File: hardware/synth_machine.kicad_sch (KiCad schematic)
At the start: 93 parts, among them J1 USB-C (MIDI + 5V power), J10 Pot WAV (10k lin, panel) JST-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, J11 Pot ATK (10k lin, panel) JST-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, J12 Pot DEC (10k lin, panel) JST-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, J13 Pot SUS (10k lin, panel) JST-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, J14 Pot REL (10k lin, panel) JST-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, J5 Speaker L (JST-PH), J6 Speaker R (JST-PH), J7 Headphones 3.5mm (CUI SJ1-351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, J8 Expansion, K1 KEY C4 (direct D10) JST-XH, K10 A4 [c2 r2] JST-XH, K11 A#4 [c1 r1] JST-XH, K12 B4 [c1 r2] JST-XH, K13 C5 [c0 r2] JST-XH, K14 BTN1 [c0 r0] JST-XH, K15 BTN2 [c0 r1] JST-XH, K16 BTN3 [c1 r0] JST-XH, K17 BTN4 [c2 r0] JST-XH, K18 BTN5 [c3 r0] JST-XH, K19 BTN6 [c4 r0] JST-XH, K2 C#4 [c5 r0] JST-XH, K3 D4 [c5 r1] JST-XH, K4 D#4 [c4 r1] JST-XH, K5 E4 [c5 r2] JST-XH, K6 F4 [c4 r2] JST-XH, K7 F#4 [c3 r1] JST-XH, K8 G4 [c3 r2] JST-XH, K9 G#4 [c2 r1] JST-XH, Q1 MMBT3904, U1 Daisy Seed / Seed3, U2 TPA6138A2PWR, U3 MAX98306ETD+T

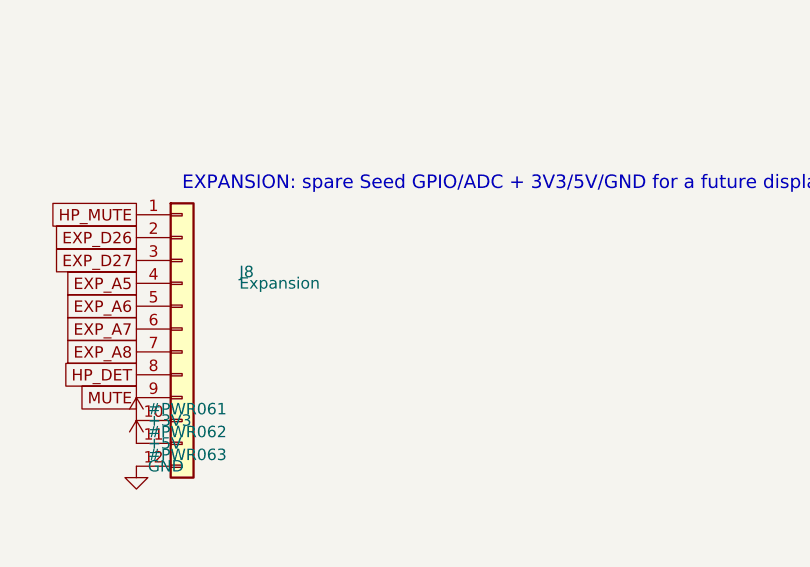
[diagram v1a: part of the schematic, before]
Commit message: J8 expansion header becomes a 1x12 female socket; Digi-Key list sized for two boards
Co-Authored-By: Claude Fable 5.1 <noreply@anthropic.com>
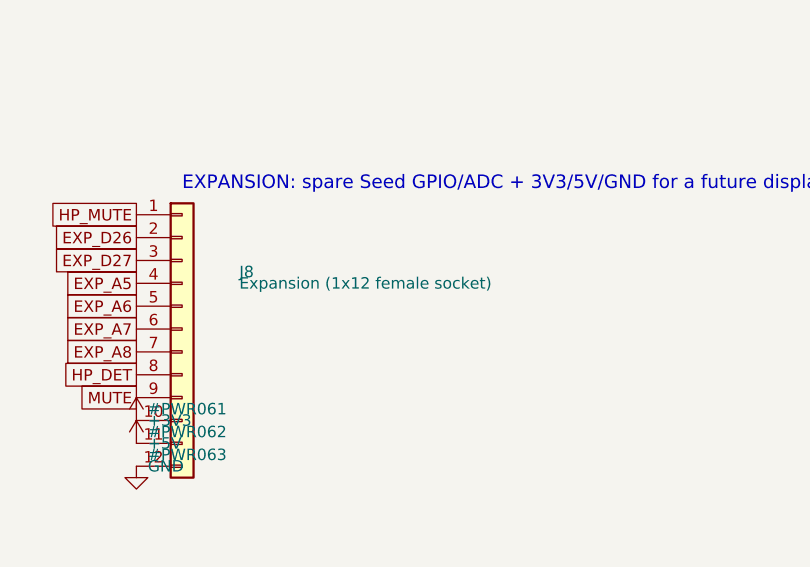
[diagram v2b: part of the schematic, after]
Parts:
- J8: value Expansion -> Expansion (1x12 female socket); footprint Connector_PinHeader_2.54mm:PinHeader_1x12_P2.54mm_Vertical -> Connector_PinSocket_2.54mm:PinSocket_1x12_P2.54mm_Vertical

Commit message: Keep the J8 pin-header footprint; Digi-Key list sized for two boards with female sockets for J8
Board files restored to the eda5d51 state (identical to what was uploaded to
JLCPCB); a 1x12 female socket solders into the same holes.

Co-Authored-By: Claude Fable 5.1 <noreply@anthropic.com>
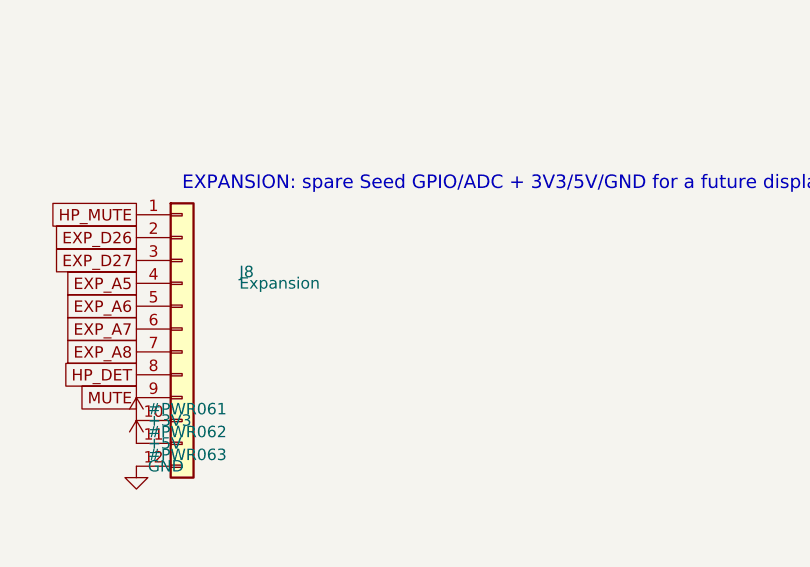
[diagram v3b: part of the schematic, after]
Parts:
- J8: value Expansion (1x12 female socket) -> Expansion; footprint Connector_PinSocket_2.54mm:PinSocket_1x12_P2.54mm_Vertical -> Connector_PinHeader_2.54mm:PinHeader_1x12_P2.54mm_Vertical
